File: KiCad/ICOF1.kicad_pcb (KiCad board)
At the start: 2 copper layers, 347.1 x 156.6 mm, 94 parts, among them J1 USB C Connector, SW1 Boot, SW10 Right, SW4 L, SW6 Left, SW8 Down, U1 XC6206, U2 USBLC6-2SC6, U3 RP2040, U4 W25Q128JVS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

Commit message: v1.2!
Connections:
- SW1 pad A: (no net) -> GND
- SW1 pad B: (no net) -> GND
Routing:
- net GND: track 49.2 -> 55.2 mm
- net +3V3: track 59.1 -> 63.3 mm, vias 3 -> 5
- net M1: track 126.9 -> 130.0 mm
- net START: track 59.6 -> 58.9 mm

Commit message: ayo!
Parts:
- removed JP10, JP11, JP12, JP13, JP14, JP15, JP16, JP17, JP18, JP19, JP2, JP20, JP21, JP3, JP4, JP5, JP6, JP7, JP8, JP9: PINHD-1X1, OF1 v1:1X01
- removed U$6: MX-B, OF1 v1:MX-BOTH
- added SW28: M1, marbastlib-mx:SW_MX_HS_1u_Htangl, B.Cu at (139.7, 145.6)
- SW1: footprint phlob2000020000:SW_TS-1187A-B-A-B -> bootsel:SW_SPST_SKQG_WithStem
- SW10, SW4, SW6, SW8: footprint OF1 v1:MX-BOTH -> marbastlib-mx:SW_MX_HS_1u_Htangl; moved to B.Cu
- SW12: renamed from U$9; value MX-B -> R; footprint OF1 v1:MX-BOTH -> marbastlib-mx:SW_MX_HS_1u_Htangl; moved to B.Cu
- SW14: renamed from U$10; value MX-B -> Y; footprint OF1 v1:MX-BOTH -> marbastlib-mx:SW_MX_HS_1u_Htangl; moved to B.Cu
- SW17: renamed from U$11; value MX-B -> LS; footprint OF1 v1:MX-BOTH -> marbastlib-mx:SW_MX_HS_1u_Htangl; moved to B.Cu
- SW19: renamed from U$12; value MX-B -> MS; footprint OF1 v1:MX-BOTH -> marbastlib-mx:SW_MX_HS_1u_Htangl; moved to B.Cu
- SW21: renamed from U$13; value MX-B -> B; footprint OF1 v1:MX-BOTH -> marbastlib-mx:SW_MX_HS_1u_Htangl; moved to B.Cu
- SW22: renamed from U$14; value MX-B -> X; footprint OF1 v1:MX-BOTH -> marbastlib-mx:SW_MX_HS_1u_Htangl; moved to B.Cu
- SW25: renamed from U$15; value MX-B -> Z; footprint OF1 v1:MX-BOTH -> marbastlib-mx:SW_MX_HS_1u_Htangl; moved to B.Cu
- SW26: renamed from U$16; value MX-B -> UP; footprint OF1 v1:MX-BOTH -> marbastlib-mx:SW_MX_HS_1u_Htangl; moved to B.Cu
- SW3: renamed from U$8; value MX-B -> Start; footprint OF1 v1:MX-BOTH -> marbastlib-mx:SW_MX_HS_1u_Htangl; moved to B.Cu
- SW30: renamed from U$7; value MX-B -> M2; footprint OF1 v1:MX-BOTH -> marbastlib-mx:SW_MX_HS_1u_Htangl; moved to B.Cu
- SW32: renamed from U$18; value MX-B -> C_LT; footprint OF1 v1:MX-BOTH -> marbastlib-mx:SW_MX_HS_1u_Htangl; moved to B.Cu
- SW35: renamed from U$17; value MX-B -> C_UP; footprint OF1 v1:MX-BOTH -> marbastlib-mx:SW_MX_HS_1u_Htangl; moved to B.Cu
- SW36: renamed from U$21; value MX-B -> C_DN; footprint OF1 v1:MX-BOTH -> marbastlib-mx:SW_MX_HS_1u_Htangl; moved to B.Cu
- SW38: renamed from U$20; value MX-B -> A; footprint OF1 v1:MX-BOTH -> marbastlib-mx:SW_MX_HS_1u_Htangl; moved to B.Cu
- SW40: renamed from U$19; value MX-B -> C_RT; footprint OF1 v1:MX-BOTH -> marbastlib-mx:SW_MX_HS_1u_Htangl; moved to B.Cu
- moved R1 4.57 mm to (218.1, 30.8)
- moved R3 2.67 mm to (214.8, 32.2), turned to 180 degrees
- moved D3 1.05 mm to (224.5, 52.0)
- moved U4 0.99 mm to (202.0, 43.1)
- moved C3 0.98 mm to (207.8, 41.3)
- moved R4 0.82 mm to (220.8, 52.1)
- moved R2 0.66 mm to (206.7, 33.5)
- moved R10 0.66 mm to (198.4, 39.1)
- moved SW1 0.55 mm to (200.3, 33.5)
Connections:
- SW30 pad : (no net) -> GND
- SW32 pad : (no net) -> GND
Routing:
- net DATA: track 51.2 -> 56.1 mm
- net +3V3: track 63.3 -> 58.7 mm, vias 5 -> 2
- net R: track 95.2 -> 97.5 mm
- net Net-(J1-SHIELD): track 25.9 -> 28.1 mm
- net Y: track 127.9 -> 129.6 mm
- net GND: track 55.2 -> 56.9 mm, vias 121 -> 120
- net 3vCable: track 36.2 -> 37.7 mm
- net QSPI_CLK: track 9.59 -> 8.44 mm
- net SD0: track 7.86 -> 6.90 mm
- net PICO_LED: track 5.07 -> 5.92 mm
- net Net-(J1-CC1): track 11.6 -> 12.4 mm
- net SD2: track 14.6 -> 13.9 mm
- net SD3: track 10.6 -> 10.0 mm
- net CS: track 21.9 -> 21.4 mm
- added copper zone on F.Cu, net +1V1
- added copper zone on F.Cu, net +3V3
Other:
- board size 347.1 x 156.6 mm -> 347.1 x 156.5 mm
- board text added: "ICOF1 v1.1"
- board text removed: "ICOF1 v1"

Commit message: ye
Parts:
- added J2: Tag-Connect TC2030, marbastlib-various:CON_TC2030_outlined, F.Cu at (217.2, 64.9)
- added REF**: 180, phlob2000020000:R_0402_1005Metric, F.Cu at (214.9, 59.2)
- R1: footprint Resistor_SMD:R_0603_1608Metric -> Resistor_SMD:R_0402_1005Metric
- R4: footprint Resistor_SMD:R_0603_1608Metric -> phlob2000020000:R_0402_1005Metric
- moved R1 4.80 mm to (217.9, 26.0), turned to 0 degrees
- moved R3 3.56 mm to (218.4, 32.1), turned to 0 degrees
- moved R11 2.59 mm to (207.6, 61.7)
- moved R5 2.25 mm to (223.2, 49.4)
- moved R6 2.25 mm to (224.8, 49.4)
- moved Y1 2.23 mm to (206.2, 65.2)
- moved C7 2.07 mm to (202.9, 65.4)
- moved C8 1.36 mm to (210.3, 65.1)
- moved SW1 1.19 mm to (200.4, 34.6)
- moved D3 1.09 mm to (223.5, 52.6)
- moved J1 1.00 mm to (211.1, 26.3)
- moved C6 0.80 mm to (212.3, 61.4)
- moved C11 0.73 mm to (217.5, 56.2)
- moved R10 0.62 mm to (198.4, 39.7), turned to 180 degrees
- moved R4 0.59 mm to (220.4, 52.6)
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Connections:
- R1 pad 1: GND -> Net-(J1-SHIELD)
- R1 pad 2: Net-(J1-SHIELD) -> GND
- SW12 pad 2: GND -> (no net)
- SW30 pad : GND -> (no net)
- SW32 pad : GND -> (no net)
- SW6 pad 2: GND -> (no net)
- U3 pad 15: C_DN -> C_LT
- U3 pad 17: C_LT -> C_DN
- U3 pad 3: L -> START
- U3 pad 34: B -> Y
- U3 pad 35: R -> B
- U3 pad 36: Y -> R
- U3 pad 4: LEFT -> RIGHT
- U3 pad 6: RIGHT -> LEFT
- U3 pad 7: START -> L
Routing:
- net C_DN: track 151.1 -> 239.0 mm
- net DOWN: track 117.6 -> 199.9 mm
- net RIGHT: track 91.4 -> 167.7 mm
- net Y: track 129.6 -> 196.3 mm
- net LEFT: track 145.7 -> 193.8 mm
- net R: track 97.5 -> 122.6 mm
- net SWD: track 0.00 -> 24.2 mm
- net SWCLK: track 0.00 -> 24.0 mm, vias 0 -> 2
- net L: track 177.7 -> 194.6 mm
- net A: track 166.1 -> 176.9 mm
- net ~{RESET}: track 0.00 -> 10.6 mm
- net +3V3: track 58.7 -> 69.0 mm, vias 2 -> 4
- net C_LT: track 136.5 -> 143.1 mm
- net START: track 58.9 -> 64.2 mm
- net B: track 99.8 -> 104.7 mm
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
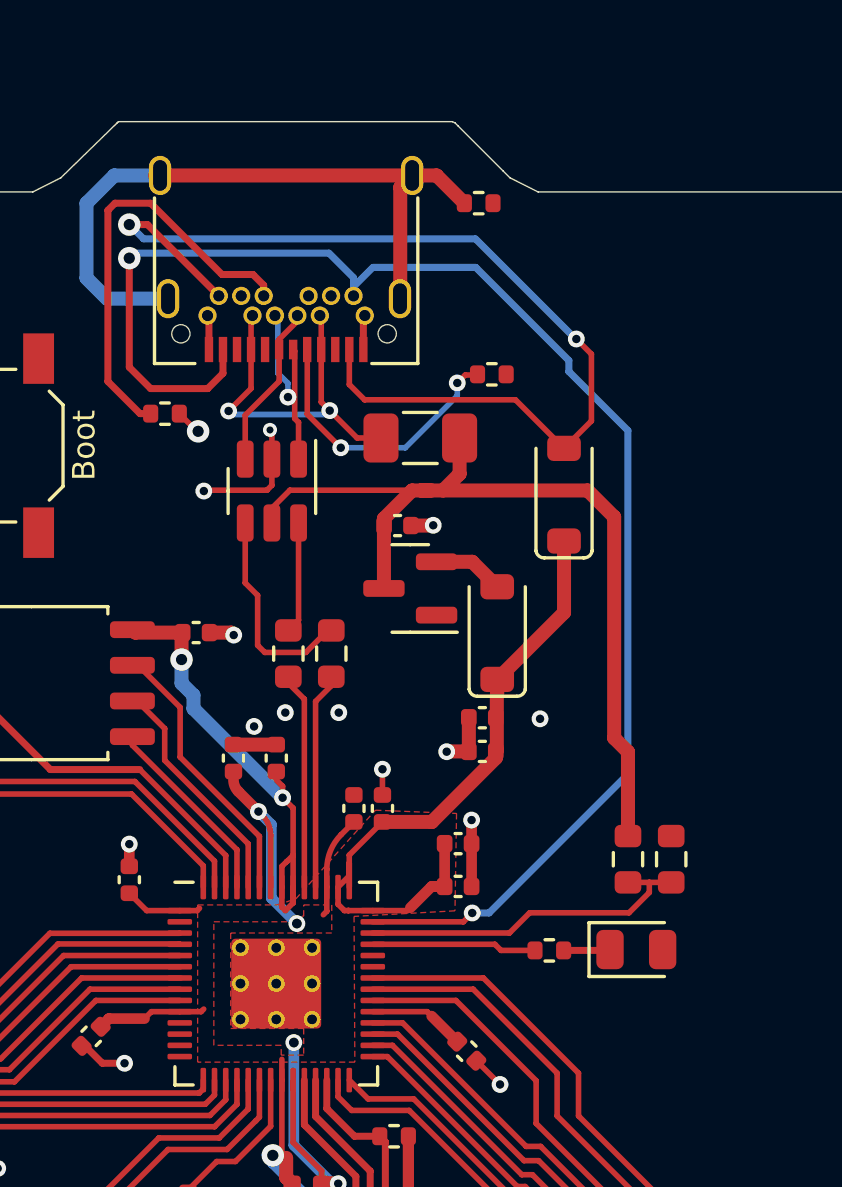
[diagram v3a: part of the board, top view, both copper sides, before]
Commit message: fixed L and R, corrected sch pinout
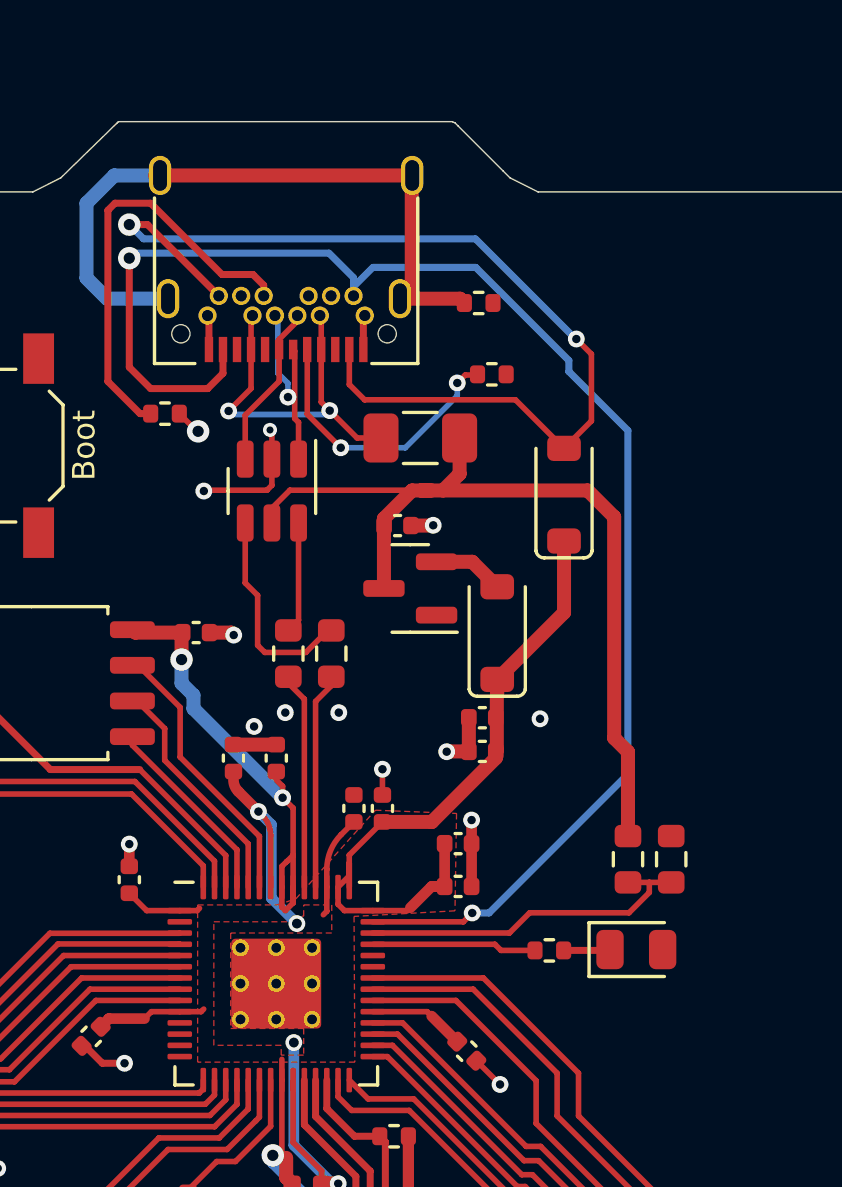
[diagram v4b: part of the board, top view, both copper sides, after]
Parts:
- moved R1 3.56 mm to (217.9, 29.6)
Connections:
- SW12 pad 2: (no net) -> GND
- SW6 pad 2: (no net) -> GND

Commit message: final
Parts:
- R1: value 1M -> 10k
- moved R3 0.84 mm to (218.9, 31.5)
- moved SW1 0.66 mm to (200.2, 34.0)
- moved R10 0.48 mm to (198.4, 39.2), turned to -90 degrees
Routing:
- net GND: track 59.2 -> 60.9 mm, vias 113 -> 114
- net Net-(J1-CC1): track 10.2 -> 11.0 mm

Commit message: final final v1.2
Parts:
- moved D3 4.61 mm to (219.7, 55.2), turned to -45 degrees
- moved R4 4.03 mm to (216.5, 53.5)
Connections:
- U3 pad 15: C_LT -> C_UP
- U3 pad 16: A -> C_LT
- U3 pad 17: C_DN -> A
- U3 pad 18: C_RT -> C_DN
- U3 pad 2: unconnected-(U3-Pad2) -> START
- U3 pad 27: C_UP -> C_RT
- U3 pad 3: START -> unconnected-(U3-Pad3)
- U3 pad 35: B -> unconnected-(U3-Pad35)
- U3 pad 36: R -> unconnected-(U3-Pad36)
- U3 pad 37: unconnected-(U3-GPIO25-Pad37) -> PICO_LED
- U3 pad 38: unconnected-(U3-GPIO26/ADC0-Pad38) -> B
- U3 pad 39: PICO_LED -> R
- U3 pad 40: VBUS_SENSE -> DATA
- U3 pad 41: DATA -> VBUS_SENSE
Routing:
- net C_DN: track 239.0 -> 145.7 mm
- net C_UP: track 107.0 -> 159.7 mm, vias 0 -> 2
- net C_RT: track 182.2 -> 144.9 mm, vias 0 -> 1
- net START: track 64.2 -> 76.9 mm
- net GND: track 60.9 -> 68.7 mm, vias 114 -> 115
- net A: track 176.9 -> 172.8 mm, vias 0 -> 2
- net PICO_LED: track 5.85 -> 1.95 mm
- net R: track 122.6 -> 125.4 mm
- net B: track 104.7 -> 107.4 mm
- net M1: track 131.3 -> 129.1 mm
- net C_LT: track 143.1 -> 141.6 mm, vias 0 -> 2
- net DATA: track 53.9 -> 55.0 mm
- net Net-(D3-A): track 1.66 -> 2.49 mm
- net RIGHT: track 167.7 -> 168.4 mm
- net DOWN: track 199.9 -> 200.7 mm
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
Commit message: v1.5
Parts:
- added G: LOGO, LOGO, F.Cu at (375.3, 164.2)
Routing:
- net A: track 172.8 -> 172.2 mm
- net C_RT: vias 1 -> 0
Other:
- board text added: "ICOF1 v1.5"
- board text added: "github.com/plants-tech/ICOF1"
- board text removed: "ICOF1 v1.1"
